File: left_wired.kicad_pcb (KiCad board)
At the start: 2 copper layers, 148.2 x 107.5 mm, 55 parts

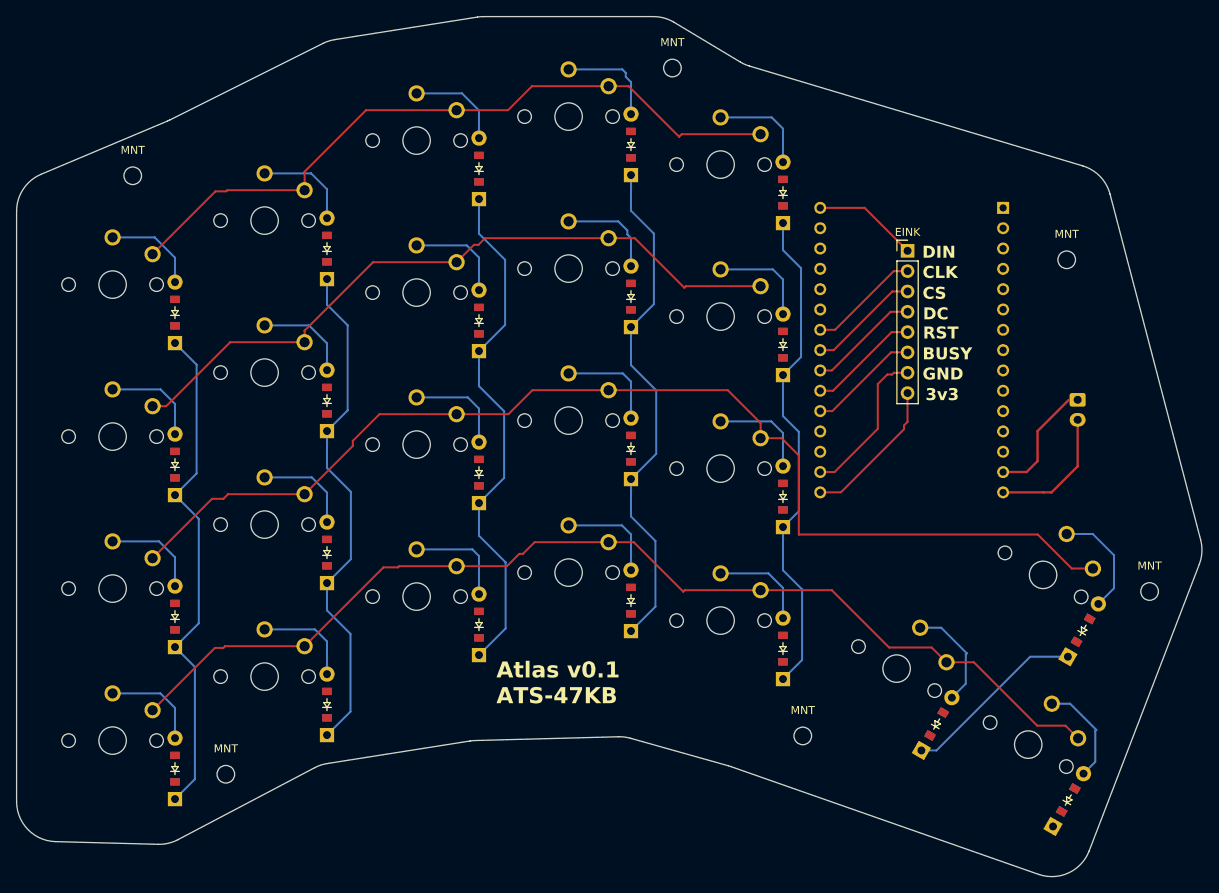
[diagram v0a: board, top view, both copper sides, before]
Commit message: Wired pcbs for row/column scanning
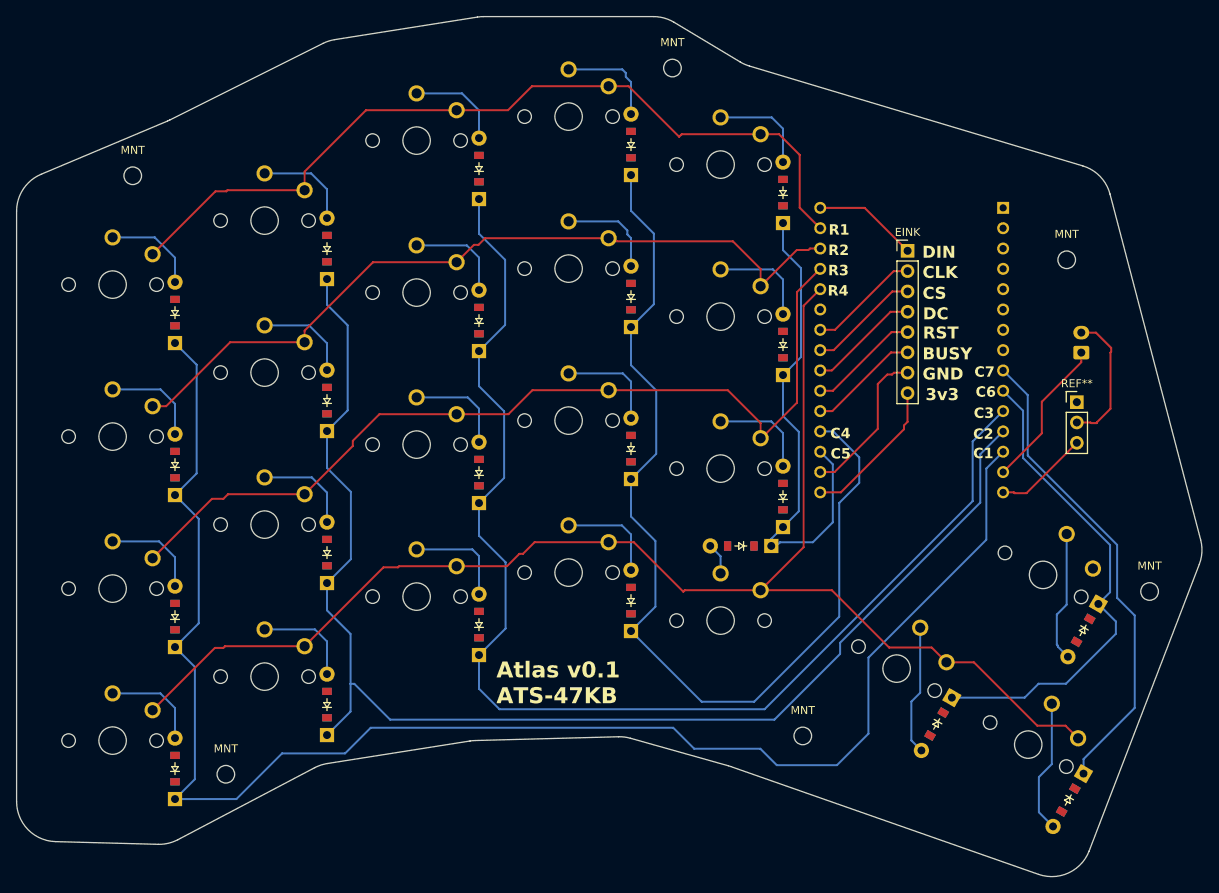
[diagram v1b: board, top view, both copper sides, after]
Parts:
- added REF**: PinHeader_1x03_P2.54mm_Vertical, Connector_PinHeader_2.54mm:PinHeader_1x03_P2.54mm_Vertical, F.Cu at (120.5, -42.3)
- moved D17 13.9 mm to (78.5, -24.3), turned to 180 degrees
- moved BAT 5.92 mm to (121.1, -48.5), turned to 90 degrees
- turned D21 to -120 degrees
- turned D22 to -120 degrees
- turned D23 to -120 degrees
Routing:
- net (no net): track 719.0 -> 1218.4 mm
- net fifth_mods: track 12.3 -> 66.2 mm
- net fourth_bottom: track 155.5 -> 125.0 mm
- net fourth_home: track 100.6 -> 111.0 mm
- net pinky_bottom: track 13.1 -> 16.7 mm
- net macro_bottom: track 13.5 -> 16.3 mm
- net ring_bottom: track 13.9 -> 16.4 mm
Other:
- board text added: "C1"
- board text added: "C2"
- board text added: "C3"
- board text added: "C4"
- board text added: "C5"
- board text added: "C6"
- board text added: "C7"
- board text added: "R1"
- board text added: "R2"
- board text added: "R3"
- board text added: "R4"

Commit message: Updated diod placement
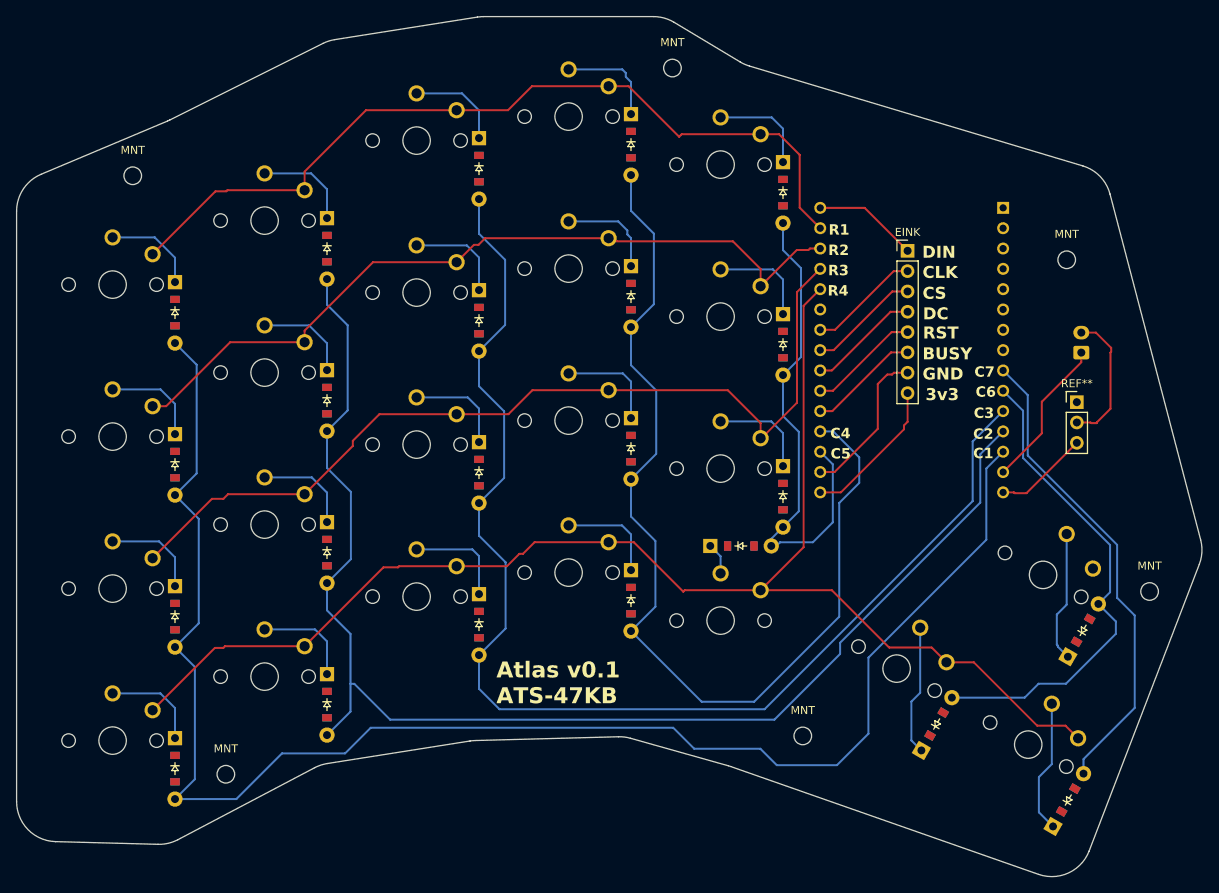
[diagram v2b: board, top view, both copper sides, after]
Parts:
- turned D1 to -90 degrees
- turned D10 to -90 degrees
- turned D11 to -90 degrees
- turned D12 to -90 degrees
- turned D13 to -90 degrees
- turned D14 to -90 degrees
- turned D15 to -90 degrees
- turned D16 to -90 degrees
- turned D17 to 0 degrees
- turned D18 to -90 degrees
- turned D19 to -90 degrees
- turned D2 to -90 degrees
- turned D20 to -90 degrees
- turned D21 to 60 degrees
- turned D22 to 60 degrees
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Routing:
- net (no net): track 1218.4 -> 1158.5 mm
- net pinky_bottom: track 16.7 -> 76.6 mm
